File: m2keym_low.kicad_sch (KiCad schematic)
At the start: 14 parts, among them J5 Bus_M.2_MDT180M03001

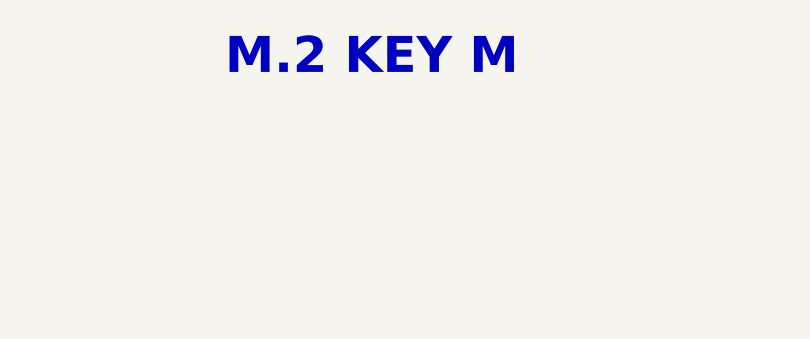
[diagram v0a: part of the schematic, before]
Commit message: [#70030] Unify functional block names
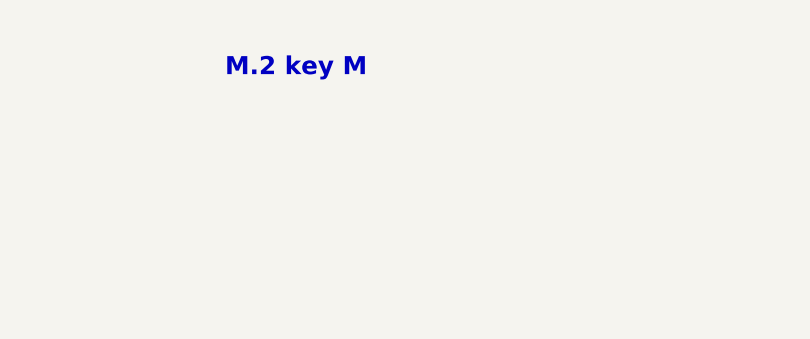
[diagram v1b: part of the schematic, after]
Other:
- note added: "M.2 key M"
- note removed: "M.2 KEY M"
- company: Antmicro Ltd. -> Antmicro Ltd
- title: Com Express 7 baseboard -> COM Express 7 Baseboard
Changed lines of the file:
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@@
 	(paper "A3")
 	(title_block
-		(title "Com Express 7 baseboard")
-		(date "2024-03-28")
+		(title "COM Express 7 Baseboard")
+		(date "2024-12-13")
 		(rev "1.1.0")
-		(company "Antmicro Ltd.")
+		(company "Antmicro Ltd")
+		(comment 1 "www.antmicro.com")
 	)
 	(junction
@@
 		)
 	)
-	(text "M.2 KEY M"
+	(text "M.2 key M"
 		(exclude_from_sim no)
 		(at 198.12 27.94 0)
 		(effects
 			(font
-				(size 4 4)
+				(size 2 2)
 				(thickness 0.8)
 				(bold yes)
